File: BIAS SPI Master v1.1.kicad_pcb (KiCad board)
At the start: 2 copper layers, 127 x 77.2 mm, 32 parts, among them J1 Apple ][ Peripheral Connector, J2 SPI Ouput, J3 GND, U1 74LS541, U2 74LS595, U3 74LS165, U4 74LS163, U5 74LS138, U6 74LS00, U7 74LS540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

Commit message: fixed a couple of typos
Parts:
- J2: value SPI Ouput -> SPI Output
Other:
- board text removed: "This is my first PCB and Tom Lemense helped tremendously. He's an awesome dude!"
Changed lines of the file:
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@@
   (general
     (thickness 1.6)
-    (drawings 35)
+    (drawings 34)
     (tracks 713)
     (zones 0)
@@
       (effects (font (size 2.032 2.032) (thickness 0.3048)))
     )
-    (fp_text value "SPI Ouput" (at 11.43 8.89 90) (layer F.SilkS)
+    (fp_text value "SPI Output" (at 11.43 8.89 90) (layer F.SilkS)
       (effects (font (size 1.778 1.778) (thickness 0.254)))
     )
@@
     )
   )
-  (gr_text "This is my first PCB and Tom Lemense helped tremendously. He's an awesome dude!" (at 134.62 110.998) (layer B.SilkS)
-    (effects (font (size 1.5 1.5) (thickness 0.3)) (justify mirror))
-  )
   (gr_poly (pts (xy 178.308 93.726) (xy 175.768 92.456) (xy 175.768 94.996)) (layer F.SilkS) (width 0.1))

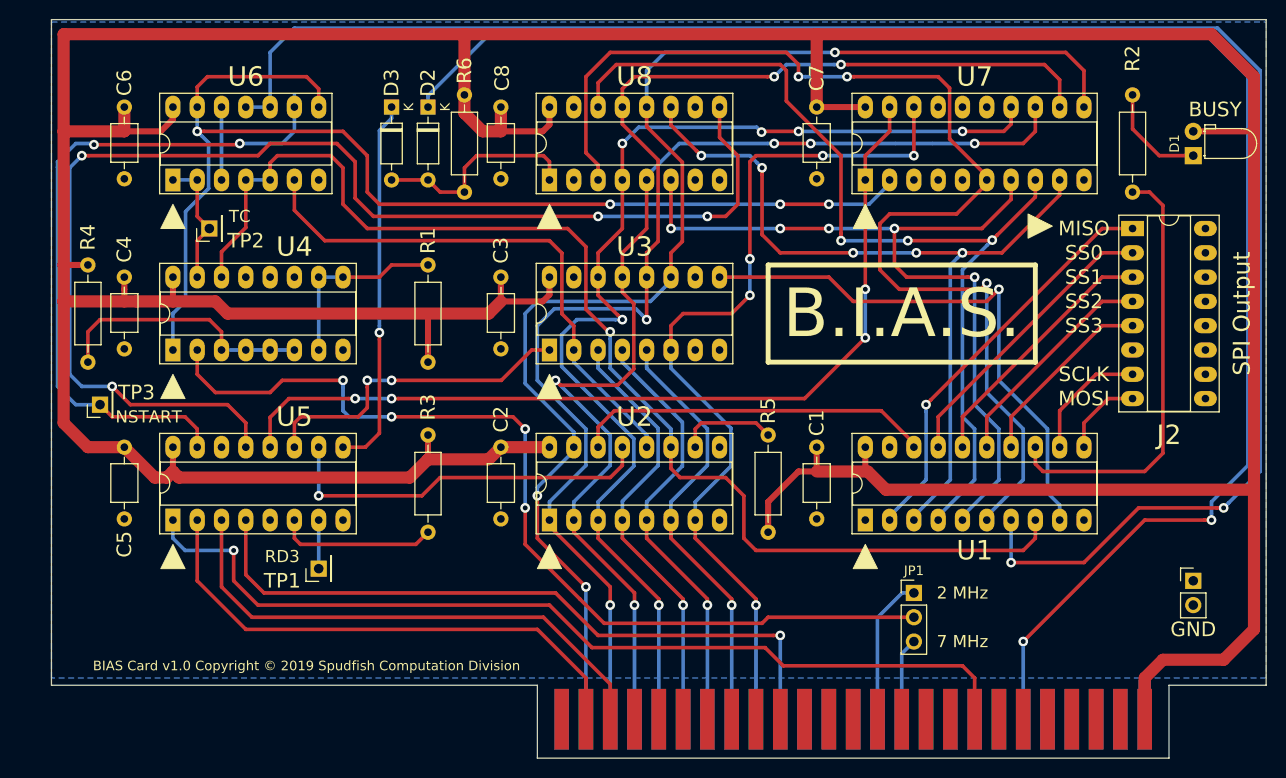
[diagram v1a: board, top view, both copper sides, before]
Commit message: Added low pass filter to clean up Apple ][ clock signal ringing
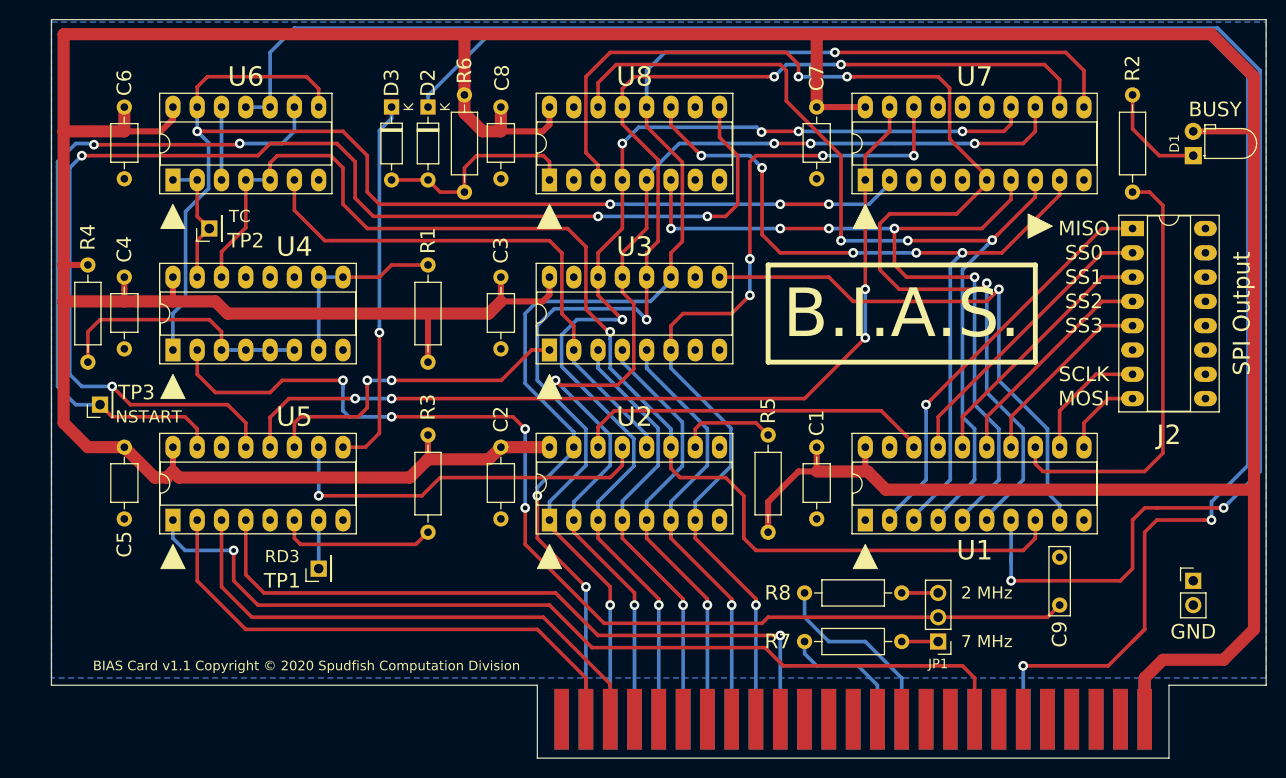
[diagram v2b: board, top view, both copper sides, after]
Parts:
- added C9: 100 pF, Capacitor_THT:C_Rect_L7.0mm_W2.0mm_P5.00mm, F.Cu at (179.1, 133.3)
- added R7: 150, Resistor_THT:R_Axial_DIN0207_L6.3mm_D2.5mm_P10.16mm_Horizontal, F.Cu at (152.4, 137.2)
- added R8: 150, Resistor_THT:R_Axial_DIN0207_L6.3mm_D2.5mm_P10.16mm_Horizontal, F.Cu at (162.6, 132.1)
- moved JP1 5.68 mm to (166.4, 137.2), turned to 180 degrees
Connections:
- net /O_nSS0 renamed /O_~SS0
- net /O_nSS1 renamed /O_~SS1
- net /O_nSS2 renamed /O_~SS2
- net /O_nSS3 renamed /O_~SS3
- net /RnW renamed /R~W
- net /nCNT_RES renamed /~CNT_RES
- net /nDS renamed /~DS
- net /nRESET renamed /~RESET
- net /nSCK renamed /~SCK
- net /nSS0 renamed /~SS0
- net /nSS1 renamed /~SS1
- net /nSS2 renamed /~SS2
- net /nSS3 renamed /~SS3
- net /nSTART renamed /~START
- J1 pad 1: (no net) -> Net-(J1-Pad1)
- J1 pad 10: (no net) -> Net-(J1-Pad10)
- J1 pad 11: (no net) -> Net-(J1-Pad11)
- J1 pad 12: (no net) -> Net-(J1-Pad12)
- J1 pad 13: (no net) -> Net-(J1-Pad13)
- J1 pad 14: (no net) -> Net-(J1-Pad14)
- J1 pad 15: (no net) -> Net-(J1-Pad15)
- J1 pad 16: (no net) -> Net-(J1-Pad16)
- J1 pad 17: (no net) -> Net-(J1-Pad17)
- J1 pad 19: (no net) -> Net-(J1-Pad19)
- J1 pad 20: (no net) -> Net-(J1-Pad20)
- J1 pad 21: (no net) -> Net-(J1-Pad21)
- J1 pad 22: (no net) -> Net-(J1-Pad22)
- J1 pad 23: (no net) -> Net-(J1-Pad23)
- J1 pad 24: (no net) -> Net-(J1-Pad24)
- J1 pad 27: (no net) -> Net-(J1-Pad27)
- J1 pad 28: (no net) -> Net-(J1-Pad28)
- J1 pad 29: (no net) -> Net-(J1-Pad29)
- J1 pad 30: (no net) -> Net-(J1-Pad30)
- J1 pad 32: (no net) -> Net-(J1-Pad32)
- J1 pad 33: (no net) -> Net-(J1-Pad33)
- J1 pad 34: (no net) -> Net-(J1-Pad34)
- J1 pad 35: (no net) -> Net-(J1-Pad35)
- J1 pad 38: (no net) -> Net-(J1-Pad38)
- J1 pad 39: (no net) -> Net-(J1-Pad39)
- J1 pad 4: (no net) -> Net-(J1-Pad4)
- J1 pad 40: (no net) -> Net-(J1-Pad40)
- J1 pad 5: (no net) -> Net-(J1-Pad5)
- J1 pad 50: (no net) -> Net-(J1-Pad50)
- J1 pad 6: (no net) -> Net-(J1-Pad6)
- J1 pad 7: (no net) -> Net-(J1-Pad7)
- J1 pad 8: (no net) -> Net-(J1-Pad8)
- J1 pad 9: (no net) -> Net-(J1-Pad9)
- JP1 pad 1: /Q3 -> Net-(JP1-Pad1)
- JP1 pad 3: /M7 -> Net-(JP1-Pad3)
- U2 pad 9: (no net) -> Net-(U2-Pad9)
- U3 pad 7: (no net) -> Net-(U3-Pad7)
- U4 pad 11: (no net) -> Net-(U4-Pad11)
- U4 pad 12: (no net) -> Net-(U4-Pad12)
- U4 pad 13: (no net) -> Net-(U4-Pad13)
- U5 pad 14: (no net) -> Net-(U5-Pad14)
- U7 pad 15: (no net) -> Net-(U7-Pad15)
- U7 pad 16: (no net) -> Net-(U7-Pad16)
- U7 pad 17: (no net) -> Net-(U7-Pad17)
- U8 pad 10: (no net) -> Net-(U8-Pad10)
- U8 pad 15: (no net) -> Net-(U8-Pad15)
- U8 pad 2: (no net) -> Net-(U8-Pad2)
- U8 pad 7: (no net) -> Net-(U8-Pad7)
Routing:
- net Net-(C9-Pad1): track 98.5 -> 114.3 mm
- net /M7: track 8.65 -> 19.6 mm
- net /~CNT_RES: track 191.0 -> 197.3 mm
- net /~RESET: track 172.4 -> 178.7 mm
- net Net-(JP1-Pad3): track 0.00 -> 3.81 mm
- net Net-(JP1-Pad1): track 0.00 -> 3.81 mm
- net /Q3: track 15.5 -> 13.8 mm
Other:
- board text added: "BIAS Card v1.1 Copyright © 2020 Spudfish Computation Division"
- board text removed: "BIAS Card v1.0 Copyright © 2019 Spudfish Computation Division"

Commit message: Fixed RC filter schematic and PCB
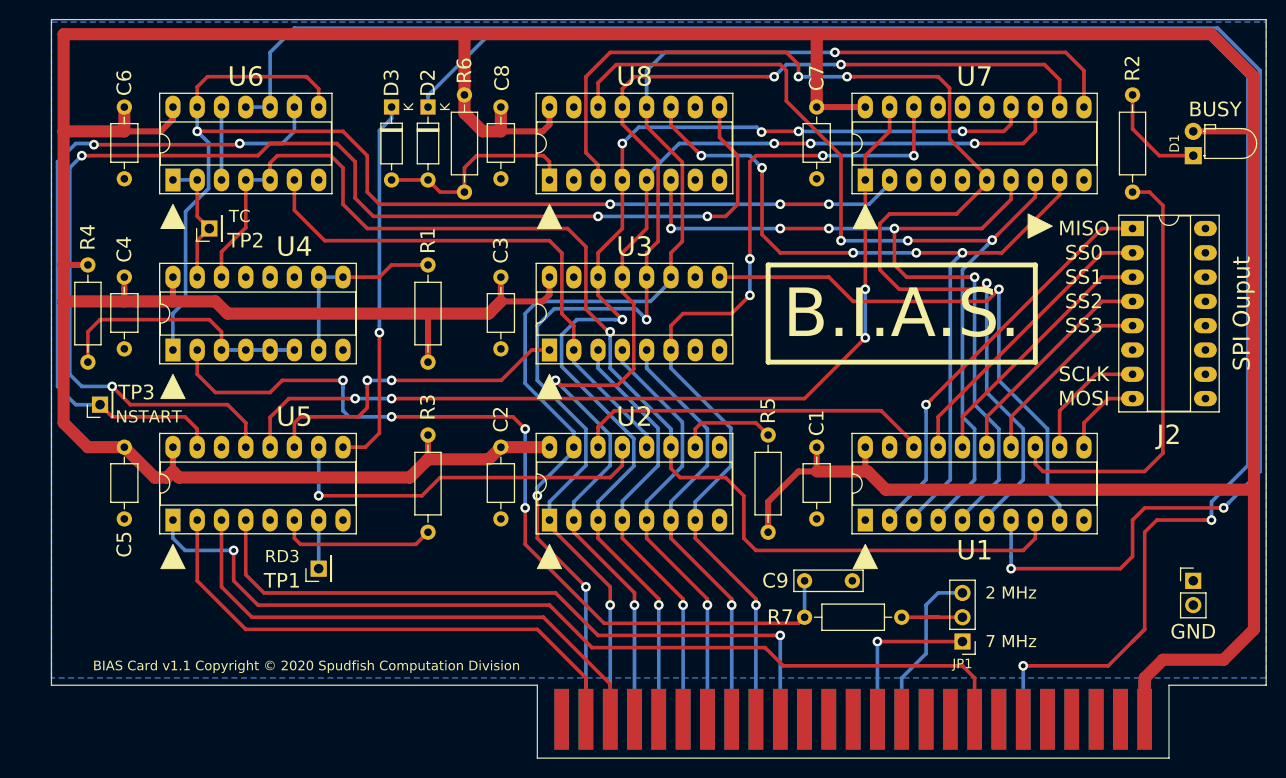
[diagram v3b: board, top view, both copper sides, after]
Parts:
- removed R8: 150, Resistor_THT:R_Axial_DIN0207_L6.3mm_D2.5mm_P10.16mm_Horizontal
- J2: value SPI Output -> SPI Ouput
- moved C9 26.8 mm to (152.4, 130.8), turned to 0 degrees
- moved R7 10.5 mm to (162.6, 134.6), turned to 180 degrees
- moved JP1 2.54 mm to (168.9, 137.2)
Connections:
- JP1 pad 1: Net-(JP1-Pad1) -> /Q3
- JP1 pad 2: Net-(C9-Pad1) -> Net-(JP1-Pad2)
- JP1 pad 3: Net-(JP1-Pad3) -> /M7
- R7 pad 1: /Q3 -> Net-(JP1-Pad2)
- R7 pad 2: Net-(JP1-Pad1) -> Net-(C9-Pad1)
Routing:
- net Net-(C9-Pad1): track 114.3 -> 90.9 mm
- net Net-(JP1-Pad2): track 0.00 -> 7.62 mm
- net Net-(JP1-Pad3): track 3.81 -> 0.00 mm
- net Net-(JP1-Pad1): track 3.81 -> 0.00 mm
- net /Q3: track 13.8 -> 17.0 mm, vias 0 -> 1
- net /~CNT_RES: track 197.3 -> 194.1 mm
- net /M7: track 19.6 -> 17.3 mm
